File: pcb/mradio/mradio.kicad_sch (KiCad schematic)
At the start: 40 parts, among them U1 STM32H745ZITx

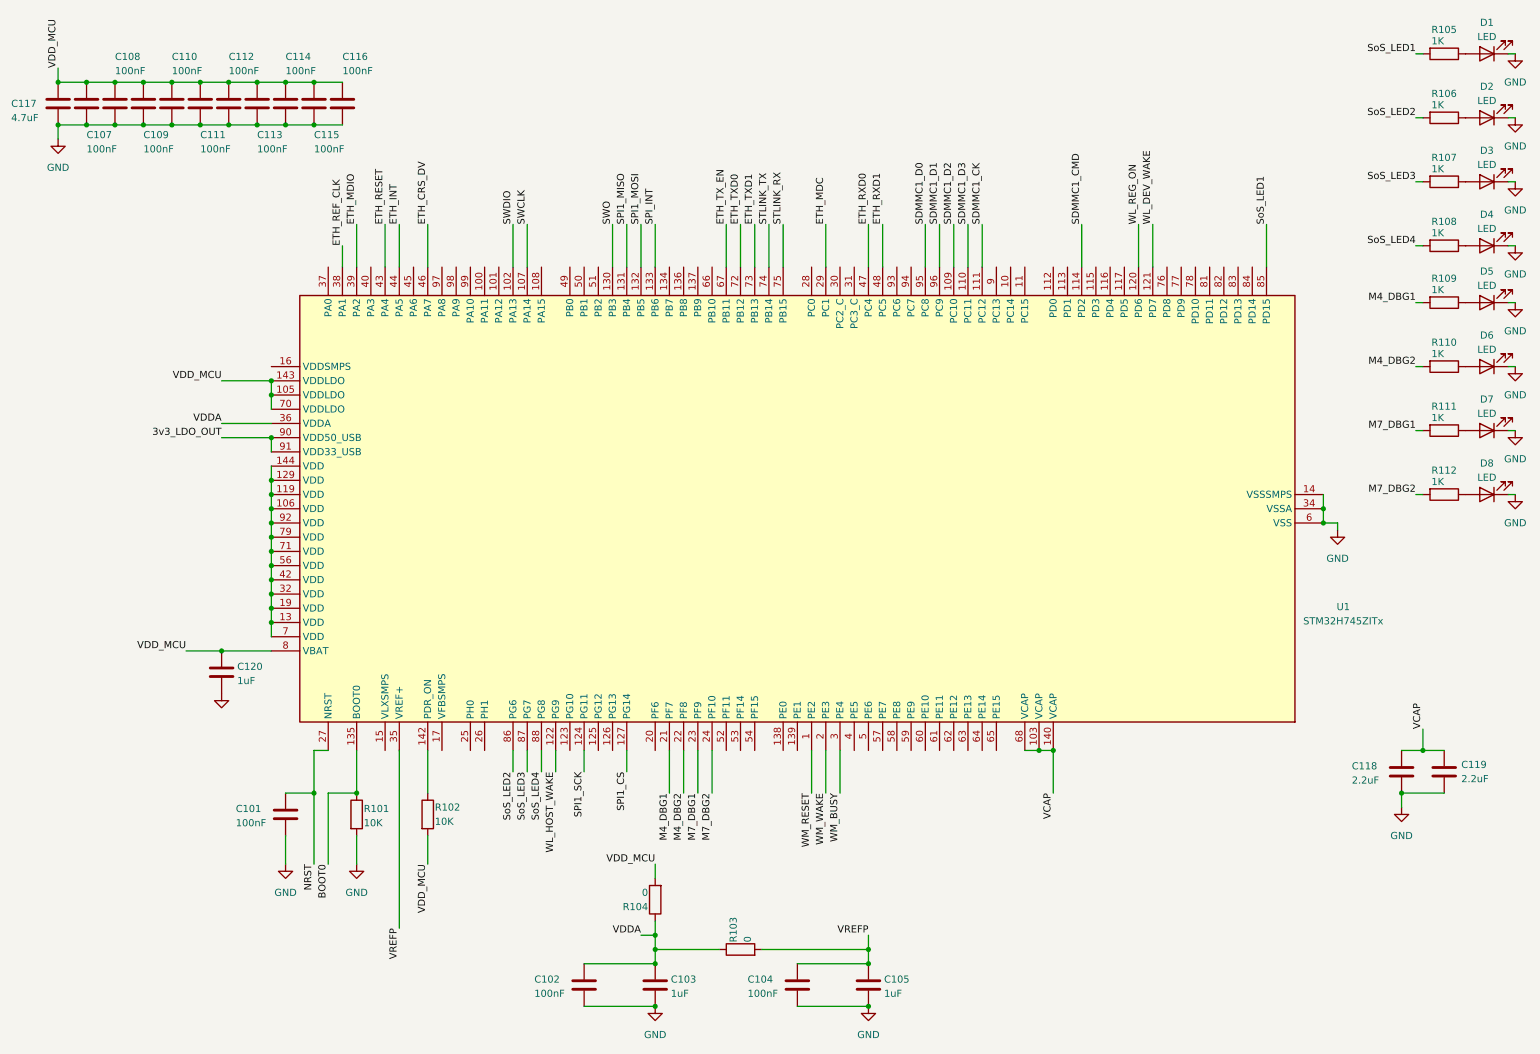
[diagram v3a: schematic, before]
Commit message: update wifi and add global labels
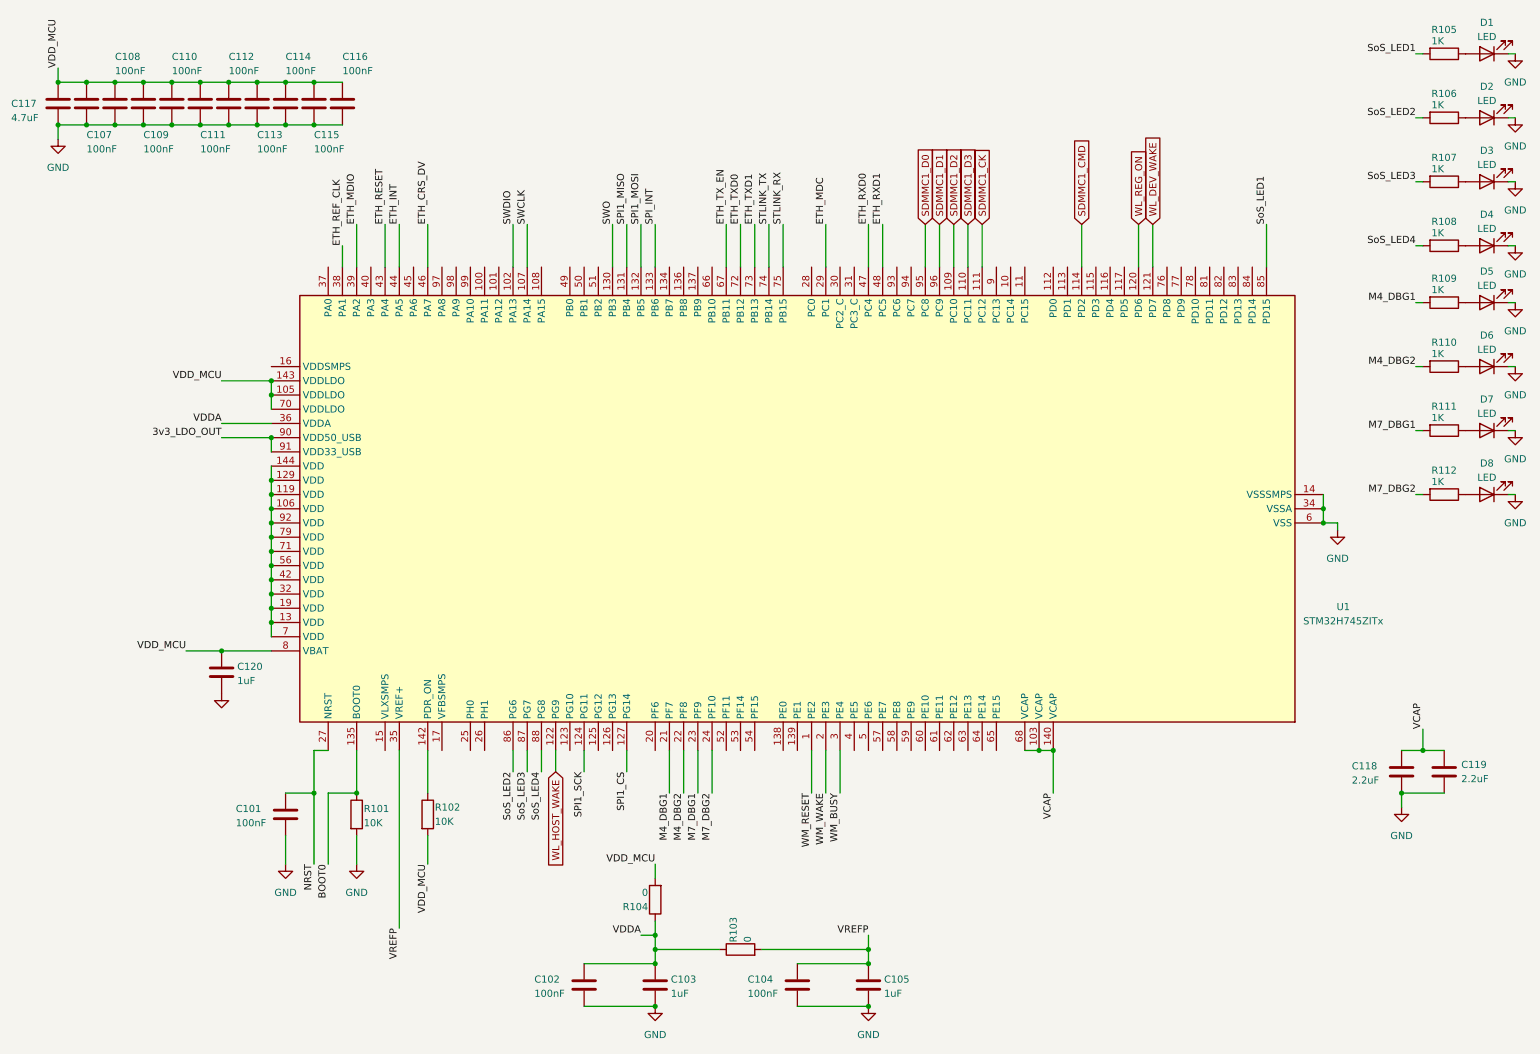
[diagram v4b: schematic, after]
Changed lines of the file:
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@@
-		)
-	)
-	(label "SDMMC1_CK"
-		(at 186.69 50.8 90)
-		(effects
-			(font
-				(size 1.27 1.27)
-			)
-			(justify left bottom)
 		)
 	)
@@
 		)
 	)
-	(label "SDMMC1_D2"
-		(at 181.61 50.8 90)
-		(effects
-			(font
-				(size 1.27 1.27)
-			)
-			(justify left bottom)
-		)
-	)
 	(label "VREFP"
 		(at 82.55 176.53 270)
@@
 		)
 	)
-	(label "WL_DEV_WAKE"
-		(at 217.17 50.8 90)
-		(effects
-			(font
-				(size 1.27 1.27)
-			)
-			(justify left bottom)
-		)
-	)
 	(label "SPI1_MISO"
 		(at 123.19 50.8 90)
@@
 		)
 	)
-	(label "WL_HOST_WAKE"
-		(at 110.49 148.59 270)
-		(effects
-			(font
-				(size 1.27 1.27)
-			)
-			(justify right bottom)
-		)
-	)
 	(label "SWCLK"
 		(at 105.41 50.8 90)
@@
 		)
 	)
-	(label "SDMMC1_CMD"
-		(at 204.47 50.8 90)
-		(effects
-			(font
-				(size 1.27 1.27)
-			)
-			(justify left bottom)
-		)
-	)
 	(label "SoS_LED1"
 		(at 237.49 50.8 90)
@@
 		)
 	)
-	(label "SDMMC1_D0"
-		(at 176.53 50.8 90)
-		(effects
-			(font
-				(size 1.27 1.27)
-			)
-			(justify left bottom)
-		)
-	)
 	(label "SWO"
 		(at 120.65 50.8 90)
@@
 		)
 	)
-	(label "SDMMC1_D3"
-		(at 184.15 50.8 90)
-		(effects
-			(font
-				(size 1.27 1.27)
-			)
-			(justify left bottom)
-		)
-	)
 	(label "ETH_REF_CLK"
 		(at 72.39 54.61 90)
@@
 		)
 	)
-	(label "SDMMC1_D1"
-		(at 179.07 50.8 90)
-		(effects
-			(font
-				(size 1.27 1.27)
-			)
-			(justify left bottom)
-		)
-	)
 	(label "VDD_MCU"
 		(at 128.27 165.1 180)
@@
 		)
 	)
-	(label "WL_REG_ON"
-		(at 214.63 50.8 90)
-		(effects
-			(font
-				(size 1.27 1.27)
-			)
-			(justify left bottom)
-		)
-	)
 	(label "BOOT0"
 		(at 69.85 165.1 270)
@@
 		)
 	)
+	(global_label "SDMMC1_D0"
+		(shape input)
+		(at 176.53 50.8 90)
+		(fields_autoplaced yes)
+		(effects
+			(font
+				(size 1.27 1.27)
+			)
+			(justify left)
+		)
+		(property "Intersheetrefs" "${INTERSHEET_REFS}"
+			(at 176.53 36.5059 90)
+			(hide yes)
+			(show_name no)
+			(do_not_autoplace no)
+			(effects
+				(font
+					(size 1.27 1.27)
+				)
+				(justify left)
+			)
+		)
+	)
+	(global_label "WL_REG_ON"
+		(shape input)
+		(at 214.63 50.8 90)
+		(fields_autoplaced yes)
+		(effects
+			(font
+				(size 1.27 1.27)
+			)
+			(justify left)
+		)
+		(property "Intersheetrefs" "${INTERSHEET_REFS}"
+			(at 214.63 37.0501 90)
+			(hide yes)
+			(show_name no)
+			(do_not_autoplace no)
+			(effects
+				(font
+					(size 1.27 1.27)
+				)
+				(justify left)
+			)
+		)
+	)
+	(global_label "WL_HOST_WAKE"
+		(shape input)
+		(at 110.49 148.59 270)
+		(fields_autoplaced yes)
+		(effects
+			(font
+				(size 1.27 1.27)
+			)
+			(justify right)
+		)
+		(property "Intersheetrefs" "${INTERSHEET_REFS}"
+			(at 110.49 165.787 90)
+			(hide yes)
+			(show_name no)
+			(do_not_autoplace no)
+			(effects
+				(font
+					(size 1.27 1.27)
+				)
+				(justify right)
+			)
+		)
+	)
+	(global_label "SDMMC1_CMD"
+		(shape input)
+		(at 204.47 50.8 90)
+		(fields_autoplaced yes)
+		(effects
+			(font
+				(size 1.27 1.27)
+			)
+			(justify left)
+		)
+		(property "Intersheetrefs" "${INTERSHEET_REFS}"
+			(at 204.47 34.994 90)
+			(hide yes)
+			(show_name no)
+			(do_not_autoplace no)
+			(effects
+				(font
+					(size 1.27 1.27)
+				)
+				(justify left)
+			)
+		)
+	)
+	(global_label "SDMMC1_D2"
+		(shape input)
+		(at 181.61 50.8 90)
+		(fields_autoplaced yes)
+		(effects
+			(font
+				(size 1.27 1.27)
+			)
+			(justify left)
+		)
+		(property "Intersheetrefs" "${INTERSHEET_REFS}"
+			(at 181.61 36.5059 90)
+			(hide yes)
+			(show_name no)
+			(do_not_autoplace no)
+			(effects
+				(font
+					(size 1.27 1.27)
+				)
+				(justify left)
+			)
+		)
+	)
+	(global_label "SDMMC1_CK"
+		(shape input)
+		(at 186.69 50.8 90)
+		(fields_autoplaced yes)
+		(effects
+			(font
+				(size 1.27 1.27)
+			)
+			(justify left)
+		)
+		(property "Intersheetrefs" "${INTERSHEET_REFS}"
+			(at 186.69 36.4454 90)
+			(hide yes)
+			(show_name no)
+			(do_not_autoplace no)
+			(effects
+				(font
+					(size 1.27 1.27)
+				)
+				(justify left)
+			)
+		)
+	)
+	(global_label "SDMMC1_D3"
+		(shape input)
+		(at 184.15 50.8 90)
+		(fields_autoplaced yes)
+		(effects
+			(font
+				(size 1.27 1.27)
+			)
+			(justify left)
+		)
+		(property "Intersheetrefs" "${INTERSHEET_REFS}"
+			(at 184.15 36.5059 90)
+			(hide yes)
+			(show_name no)
+			(do_not_autoplace no)
+			(effects
+				(font
+					(size 1.27 1.27)
+				)
+				(justify left)
+			)
+		)
+	)
+	(global_label "WL_DEV_WAKE"
+		(shape input)
+		(at 217.17 50.8 90)
+		(fields_autoplaced yes)
+		(effects
+			(font
+				(size 1.27 1.27)
+			)
+			(justify left)
+		)
+		(property "Intersheetrefs" "${INTERSHEET_REFS}"
+			(at 217.17 34.9335 90)
+			(hide yes)
+			(show_name no)
+			(do_not_autoplace no)
+			(effects
+				(font
+					(size 1.27 1.27)
+				)
+				(justify left)
+			)
+		)
+	)
+	(global_label "SDMMC1_D1"
+		(shape input)
+		(at 179.07 50.8 90)
+		(fields_autoplaced yes)
+		(effects
+			(font
+				(size 1.27 1.27)
+			)
+			(justify left)
+		)
+		(property "Intersheetrefs" "${INTERSHEET_REFS}"
+			(at 179.07 36.5059 90)
+			(hide yes)
+			(show_name no)
+			(do_not_autoplace no)
+			(effects
+				(font
+					(size 1.27 1.27)
+				)
+				(justify left)
+			)
+		)
+	)
